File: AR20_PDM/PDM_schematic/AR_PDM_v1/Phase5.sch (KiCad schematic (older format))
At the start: 12 parts, among them Q5 BTS50025-1TAD, U7 INA233

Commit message: Alpha version DONE! - Gerber files generated
- Tweeked
- checked and re cheked
- added all missing components
- Created a really nice silkscreen
- Ready To Test
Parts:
- renumbered C_in2 to C17, C_out2 to C18, C_vs2 to C19, Cs2 to C20, C_bypass5 to C21, Q5 to Q3, R8 to R14, R_in2 to R15, R_sense2 to R16, R_s2 to R17, R_Shunt6 to R18, U7 to U4

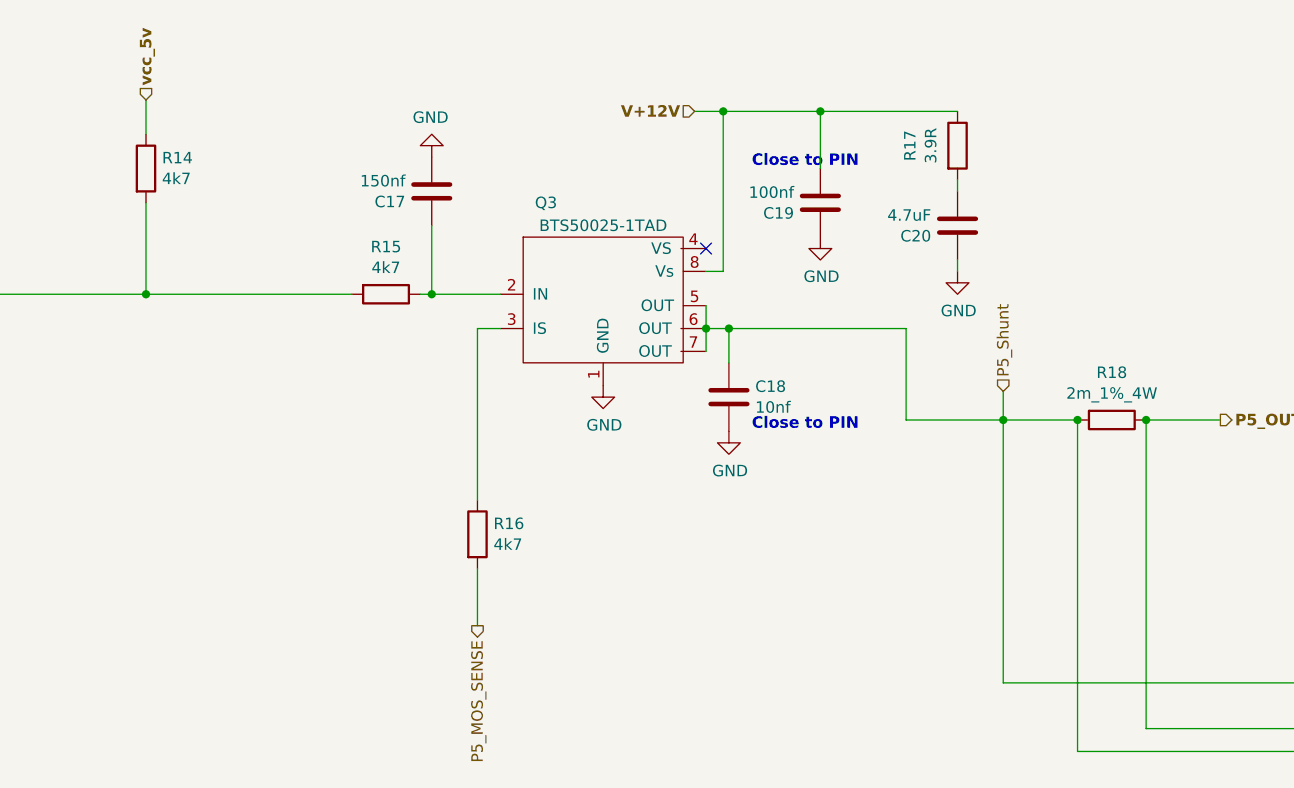
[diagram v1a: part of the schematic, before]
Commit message: Fixed wrong resistors, mos sense. Gerber files updated
- removed all R_is_protection resistors on each mosfet line
- added one R_is_protection resistors to mos_sense_all
ps, mux N-fets, does not need overvoltage protection. 60 volt tolerant.
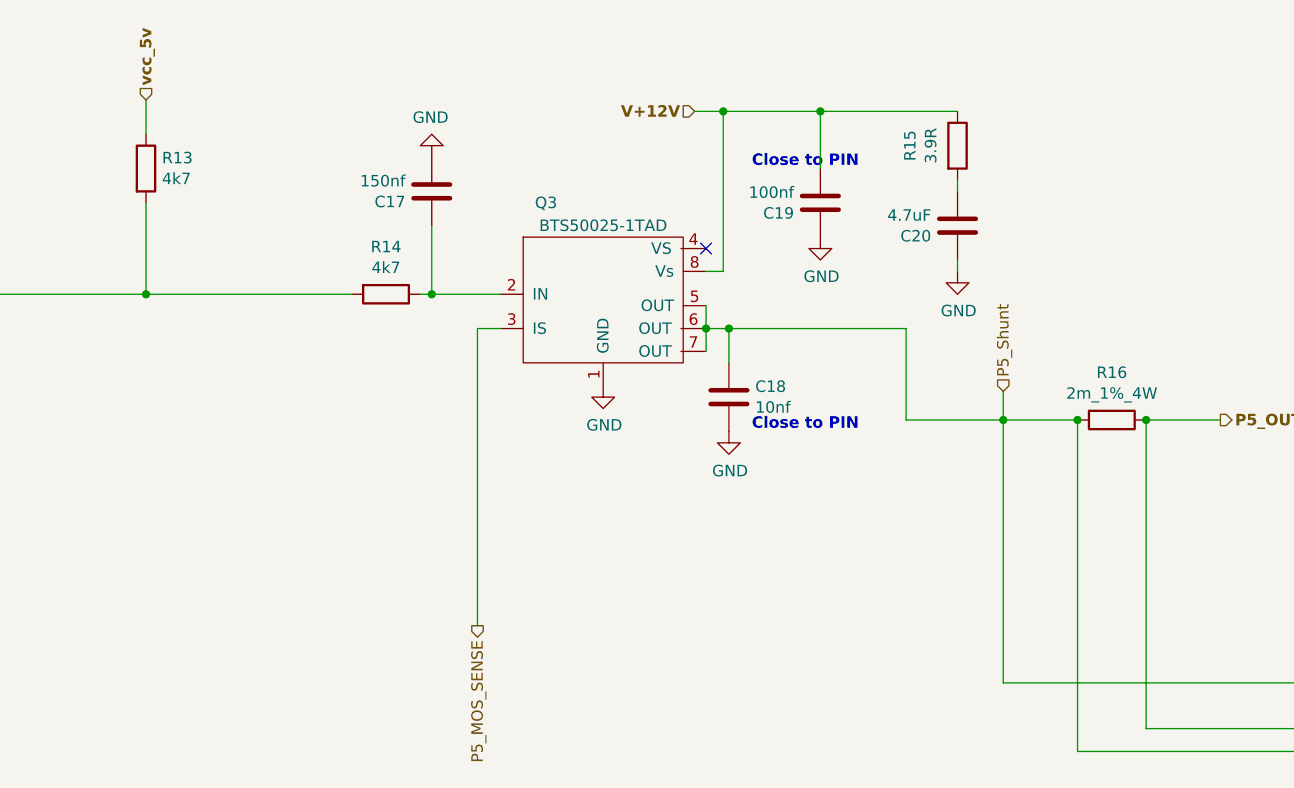
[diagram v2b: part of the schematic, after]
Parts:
- removed R16: 4k7, Resistor_SMD:R_0603_1608Metric, symbol AR20_PDM_v1-rescue:R-Device
- renumbered R14 to R13, R15 to R14, R17 to R15, R18 to R16
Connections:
- net P5_MOS_SENSE: now also Q3.3 (IS)
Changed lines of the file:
@@
 AR Path="/5E0FBBBD/5E21B80A" Ref="R?"  Part="1"
 AR Path="/5E0FC3A2/5E21B80A" Ref="R?"  Part="1"
-AR Path="/5E0FCFDC/5E21B80A" Ref="R15"  Part="1"
+AR Path="/5E0FCFDC/5E21B80A" Ref="R14"  Part="1"
 AR Path="/5E0FDCCC/5E21B80A" Ref="R?"  Part="1"
 AR Path="/5E10174B/5E21B80A" Ref="R?"  Part="1"
-F 0 "R15" V 3093 2400 50  0000 C CNN
+F 0 "R14" V 3093 2400 50  0000 C CNN
 F 1 "4k7" V 3184 2400 50  0000 C CNN
 F 2 "Resistor_SMD:R_0603_1608Metric" V 3230 2400 50  0001 C CNN
@@
 AR Path="/5E0FBBBD/5E21B81D" Ref="R?"  Part="1"
 AR Path="/5E0FC3A2/5E21B81D" Ref="R?"  Part="1"
-AR Path="/5E0FCFDC/5E21B81D" Ref="R14"  Part="1"
+AR Path="/5E0FCFDC/5E21B81D" Ref="R13"  Part="1"
 AR Path="/5E0FDCCC/5E21B81D" Ref="R?"  Part="1"
 AR Path="/5E10174B/5E21B81D" Ref="R?"  Part="1"
-F 0 "R14" H 2320 1896 50  0000 L CNN
+F 0 "R13" H 2320 1896 50  0000 L CNN
 F 1 "4k7" H 2320 1805 50  0000 L CNN
 F 2 "Resistor_SMD:R_0603_1608Metric" V 2180 1850 50  0001 C CNN
@@
 	3700 2550 3800 2550
 Wire Wire Line
-	3700 3850 3700 3600
-Wire Wire Line
 	8750 2850 8750 3350
 Wire Wire Line
@@
 AR Path="/5E0FBBBD/5E21B871" Ref="R?"  Part="1"
 AR Path="/5E0FC3A2/5E21B871" Ref="R?"  Part="1"
-AR Path="/5E0FCFDC/5E21B871" Ref="R17"  Part="1"
+AR Path="/5E0FCFDC/5E21B871" Ref="R15"  Part="1"
 AR Path="/5E0FDCCC/5E21B871" Ref="R?"  Part="1"
 AR Path="/5E10174B/5E21B871" Ref="R?"  Part="1"
-F 0 "R17" V 5593 1750 50  0000 C CNN
+F 0 "R15" V 5593 1750 50  0000 C CNN
 F 1 "3.9R" V 5684 1750 50  0000 C CNN
 F 2 "Resistor_SMD:R_0603_1608Metric" V 5730 1750 50  0001 C CNN
@@
 Wire Wire Line
 	6000 4100 8750 4100
-$Comp
-L AR20_PDM_v1-rescue:R-Device R?
-U 1 1 5E21B874
-P 3700 3450
-AR Path="/5DA89415/5E21B874" Ref="R?"  Part="1"
-AR Path="/5DEB10A1/5E21B874" Ref="R?"  Part="1"
-AR Path="/5DEB20EA/5E21B874" Ref="R?"  Part="1"
-AR Path="/5E0E4725/5E21B874" Ref="R?"  Part="1"
-AR Path="/5E0E4A93/5E21B874" Ref="R?"  Part="1"
-AR Path="/5E0E4EB5/5E21B874" Ref="R?"  Part="1"
-AR Path="/5E0E5304/5E21B874" Ref="R?"  Part="1"
-AR Path="/5E0E594B/5E21B874" Ref="R?"  Part="1"
-AR Path="/5E0E607C/5E21B874" Ref="R?"  Part="1"
-AR Path="/5E0FB5C8/5E21B874" Ref="R?"  Part="1"
-AR Path="/5E0FBBBD/5E21B874" Ref="R?"  Part="1"
-AR Path="/5E0FC3A2/5E21B874" Ref="R?"  Part="1"
-AR Path="/5E0FCFDC/5E21B874" Ref="R16"  Part="1"
-AR Path="/5E0FDCCC/5E21B874" Ref="R?"  Part="1"
-AR Path="/5E10174B/5E21B874" Ref="R?"  Part="1"
-F 0 "R16" H 3770 3496 50  0000 L CNN
-F 1 "4k7" H 3770 3405 50  0000 L CNN
-F 2 "Resistor_SMD:R_0603_1608Metric" V 3630 3450 50  0001 C CNN
-F 3 "~" H 3700 3450 50  0001 C CNN
-	1    3700 3450
-	1    0    0    -1
-$EndComp
 Wire Wire Line
 	6325 4400 8750 4400
@@
 AR Path="/5E0FBBBD/5E1D54E4" Ref="R?"  Part="1"
 AR Path="/5E0FC3A2/5E1D54E4" Ref="R?"  Part="1"
-AR Path="/5E0FCFDC/5E1D54E4" Ref="R18"  Part="1"
+AR Path="/5E0FCFDC/5E1D54E4" Ref="R16"  Part="1"
 AR Path="/5E0FDCCC/5E1D54E4" Ref="R?"  Part="1"
 AR Path="/5E10174B/5E1D54E4" Ref="R?"  Part="1"
-F 0 "R18" V 6268 2950 50  0000 C CNN
+F 0 "R16" V 6268 2950 50  0000 C CNN
 F 1 "2m_1%_4W" V 6359 2950 50  0000 C CNN
 F 2 "Resistor_SMD:R_2512_6332Metric" V 6405 2950 50  0001 C CNN
@@
 Connection ~ 6000 2950
 Wire Wire Line
-	3700 2550 3700 3300
-Wire Wire Line
 	4650 1600 4775 1600
 Wire Wire Line
@@
 Wire Wire Line
 	4775 1600 5200 1600
+Wire Wire Line
+	3700 2550 3700 3850
 $EndSCHEMATC

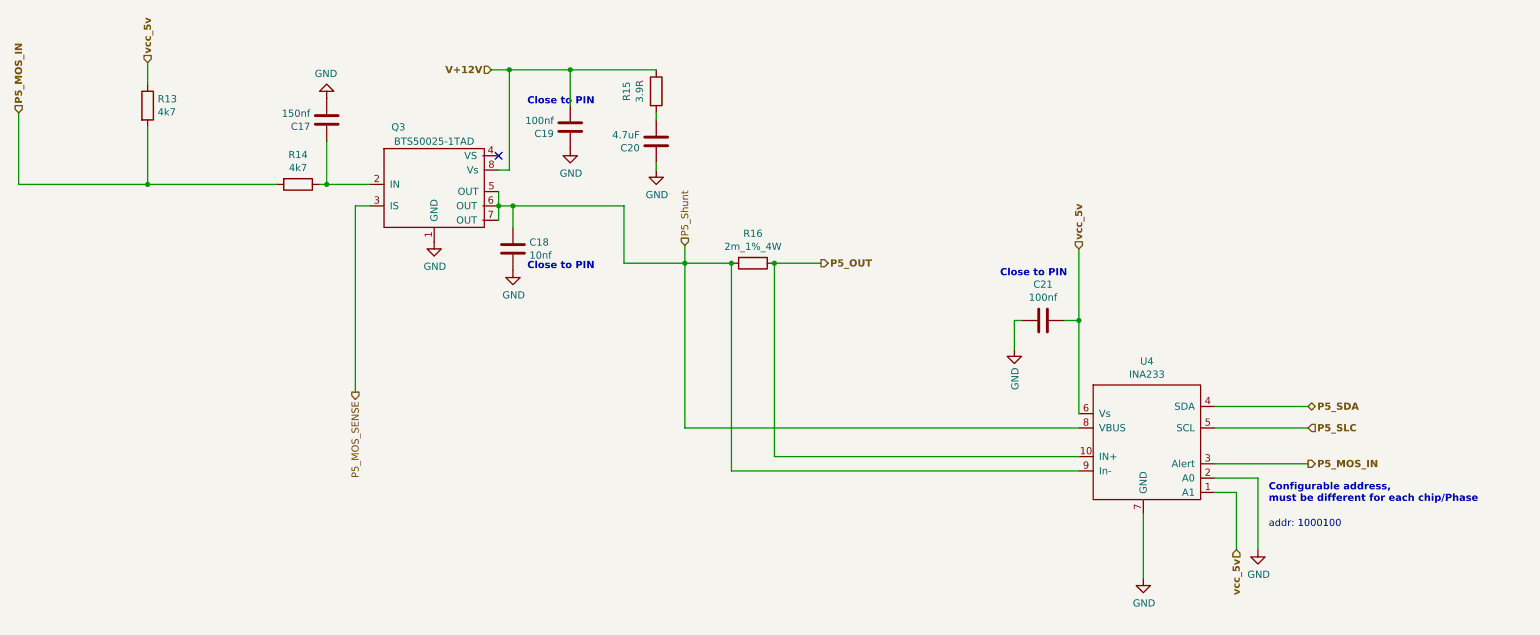
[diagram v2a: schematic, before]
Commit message: Major redesign. schematics completed, PCB work in progress
-TODO : A proper changelog file. Where all changes will apear 
- Redesigned schematics to accommodate errors in the improvement list
- More detail in ALPHA improvement list
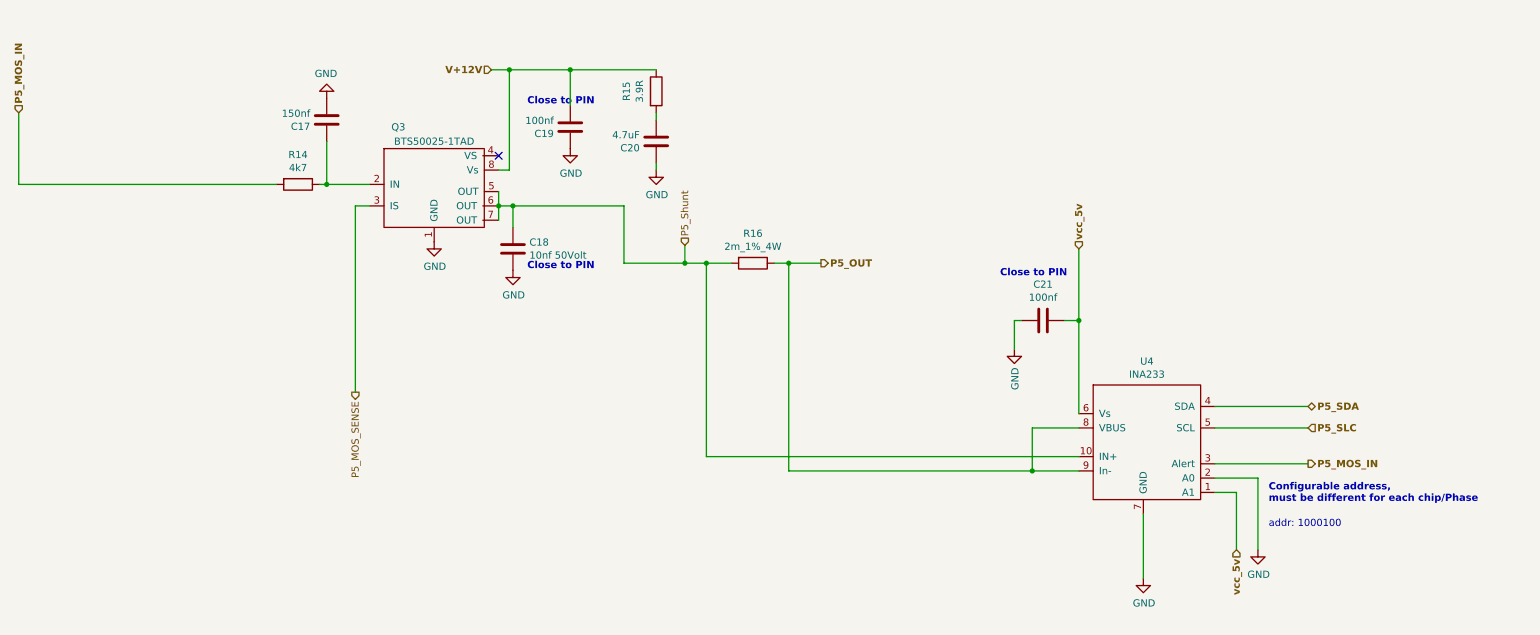
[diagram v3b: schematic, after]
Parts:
- removed R13: 4k7, Resistor_SMD:R_0603_1608Metric, symbol AR20_PDM_v1-rescue:R-Device
- C18: value 10nf -> 10nf 50Volt
- R15: footprint Resistor_SMD:R_0603_1608Metric -> Resistor_SMD:R_2512_6332Metric
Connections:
- net P5_OUT: now also U4.8 (VBUS), U4.9 (In-); no longer U4.10 (IN+)
- net P5_Shunt: now also U4.10 (IN+); no longer U4.8 (VBUS), U4.9 (In-)
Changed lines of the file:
@@
 $Descr A4 11693 8268
 encoding utf-8
-Sheet 4 13
+Sheet 4 14
 Title ""
 Date ""
@@
 AR Path="/5E10174B/5E21B810" Ref="C?"  Part="1"
 F 0 "C18" H 4915 2896 50  0000 L CNN
-F 1 "10nf" H 4915 2805 50  0000 L CNN
+F 1 "10nf 50Volt" H 4915 2805 50  0000 L CNN
 F 2 "Capacitor_SMD:C_0603_1608Metric" H 4838 2700 50  0001 C CNN
 F 3 "~" H 4800 2850 50  0001 C CNN
@@
 $EndComp
 $Comp
-L AR20_PDM_v1-rescue:R-Device R?
-U 1 1 5E21B81D
-P 2250 1850
-AR Path="/5DA89415/5E21B81D" Ref="R?"  Part="1"
-AR Path="/5DEB10A1/5E21B81D" Ref="R?"  Part="1"
-AR Path="/5DEB20EA/5E21B81D" Ref="R?"  Part="1"
-AR Path="/5E0E4725/5E21B81D" Ref="R?"  Part="1"
-AR Path="/5E0E4A93/5E21B81D" Ref="R?"  Part="1"
-AR Path="/5E0E4EB5/5E21B81D" Ref="R?"  Part="1"
-AR Path="/5E0E5304/5E21B81D" Ref="R?"  Part="1"
-AR Path="/5E0E594B/5E21B81D" Ref="R?"  Part="1"
-AR Path="/5E0E607C/5E21B81D" Ref="R?"  Part="1"
-AR Path="/5E0FB5C8/5E21B81D" Ref="R?"  Part="1"
-AR Path="/5E0FBBBD/5E21B81D" Ref="R?"  Part="1"
-AR Path="/5E0FC3A2/5E21B81D" Ref="R?"  Part="1"
-AR Path="/5E0FCFDC/5E21B81D" Ref="R13"  Part="1"
-AR Path="/5E0FDCCC/5E21B81D" Ref="R?"  Part="1"
-AR Path="/5E10174B/5E21B81D" Ref="R?"  Part="1"
-F 0 "R13" H 2320 1896 50  0000 L CNN
-F 1 "4k7" H 2320 1805 50  0000 L CNN
-F 2 "Resistor_SMD:R_0603_1608Metric" V 2180 1850 50  0001 C CNN
-F 3 "~" H 2250 1850 50  0001 C CNN
-	1    2250 1850
-	1    0    0    -1
-$EndComp
-$Comp
 L AR20_PDM_v1-rescue:C-Device C?
 U 1 1 5E21B825
@@
 Text Notes 8200 3050 0    50   ~ 10
 Close to PIN
-Text HLabel 2250 1550 1    50   Input ~ 10
-vcc_5v
 Wire Wire Line
 	9700 4100 10350 4100
-Wire Wire Line
-	2250 1550 2250 1700
 $Comp
 L AR20_PDM_v1-rescue:C-Device C?
@@
 F 0 "R15" V 5593 1750 50  0000 C CNN
 F 1 "3.9R" V 5684 1750 50  0000 C CNN
-F 2 "Resistor_SMD:R_0603_1608Metric" V 5730 1750 50  0001 C CNN
+F 2 "Resistor_SMD:R_2512_6332Metric" V 5730 1750 50  0001 C CNN
 F 3 "~" H 5800 1750 50  0001 C CNN
 	1    5800 1750
@@
 Wire Wire Line
 	9700 4350 10350 4350
-Connection ~ 2250 2400
-Wire Wire Line
-	2250 2000 2250 2400
 Wire Wire Line
 	1350 1900 1350 2400
-Wire Wire Line
-	1350 2400 2250 2400
 Wire Wire Line
 	10000 4450 10000 4950
@@
 	5575 2550 5575 2950
 Connection ~ 4800 2550
-Wire Wire Line
-	6000 4100 8750 4100
-Wire Wire Line
-	6325 4400 8750 4400
-Wire Wire Line
-	6625 4300 8750 4300
 Text HLabel 3700 3850 3    50   Output ~ 0
 P5_MOS_SENSE
-Wire Wire Line
-	6000 4100 6000 2950
 Wire Wire Line
 	5575 2950 6000 2950
@@
 V+12V
 Wire Wire Line
-	2250 2400 3150 2400
-Wire Wire Line
-	6625 2950 6625 4300
-Wire Wire Line
-	6325 2950 6325 4400
-Wire Wire Line
-	6000 2950 6325 2950
+	6000 2950 6150 2950
 $Comp
 L AR20_PDM_v1-rescue:R-Device R?
@@
 $EndComp
 Wire Wire Line
-	6625 2950 6950 2950
-Connection ~ 6325 2950
-Connection ~ 6625 2950
+	6625 2950 6725 2950
 Wire Wire Line
 	9200 4700 9200 5150
@@
 Wire Wire Line
 	3700 2550 3700 3850
+Wire Wire Line
+	1350 2400 3150 2400
+Wire Wire Line
+	8750 4300 6150 4300
+Wire Wire Line
+	6150 4300 6150 2950
+Wire Wire Line
+	8750 4400 8425 4400
+Wire Wire Line
+	8750 4100 8425 4100
+Wire Wire Line
+	8425 4100 8425 4400
+Connection ~ 8425 4400
+Wire Wire Line
+	8425 4400 6725 4400
+Wire Wire Line
+	6725 4400 6725 2950
+Connection ~ 6725 2950
+Wire Wire Line
+	6725 2950 6950 2950
+Connection ~ 6150 2950
+Wire Wire Line
+	6150 2950 6325 2950
 $EndSCHEMATC

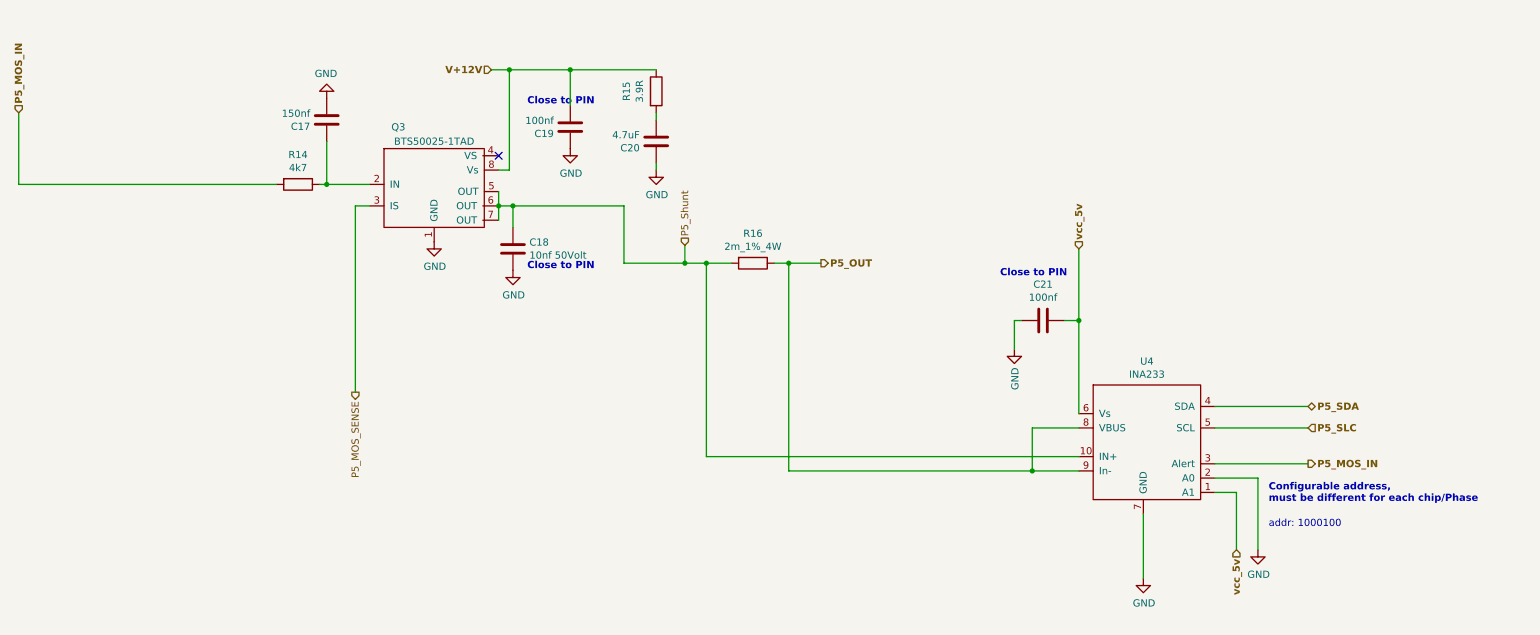
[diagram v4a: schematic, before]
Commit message: schematics rework
Fixed INA233 frying due to inductive flyback:
- Paced ina233 high side of the mosftets
- New input protection reseistors, and zener diodes, on each ina233.
Simplified:
- Removed the MUX and mos sense lines, as i realize that most of this functionality can be obtained trough INA233.
- Removed some of the cappacitors , besides the most needed ones.
- removed  back to back zener diode configuration, now a single diode insted.
 to reduce negative voltage in case of loss of VS, to be easy on the INA233 filters.
new stuff:
- Another temp sensor.
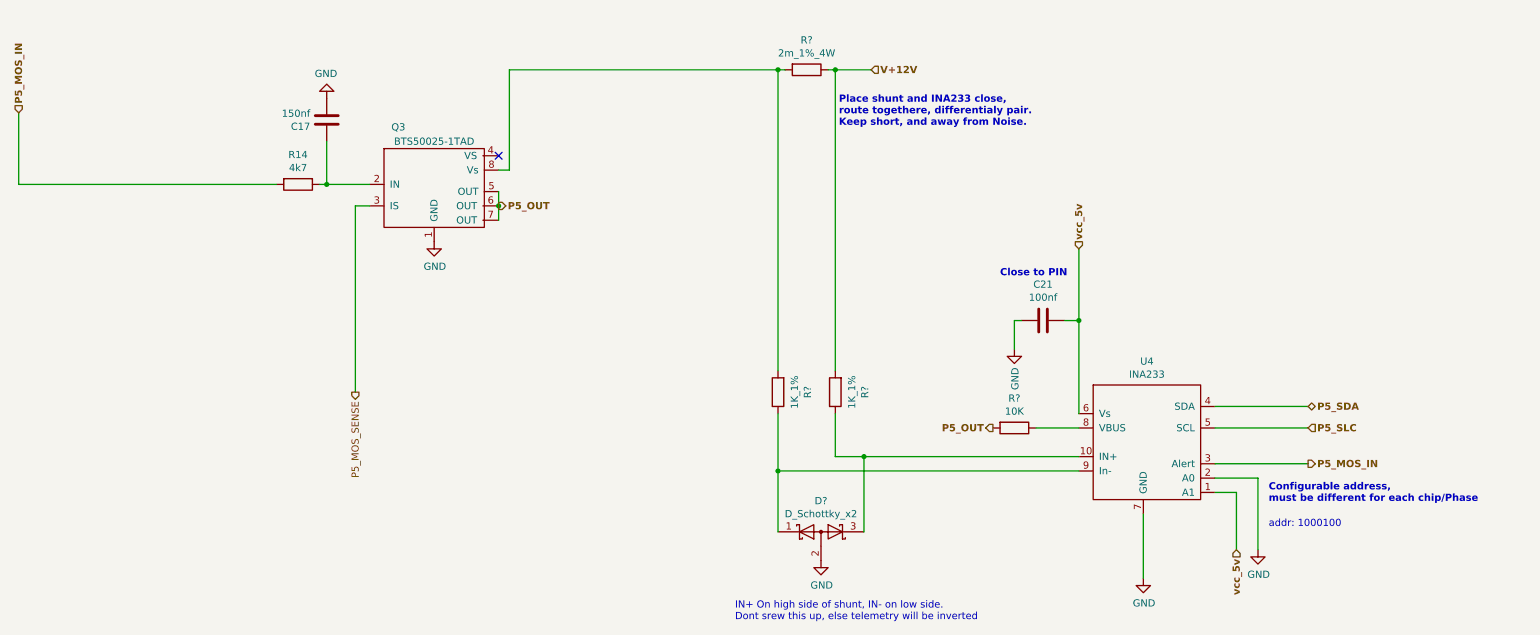
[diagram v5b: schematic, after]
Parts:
- removed C18: 10nf 50Volt, Capacitor_SMD:C_0603_1608Metric, symbol AR20_PDM_v1-rescue:C-Device
- removed C19: 100nf, Capacitor_SMD:C_0603_1608Metric, symbol AR20_PDM_v1-rescue:C-Device
- removed C20: 4.7uF, Capacitor_SMD:C_1206_3216Metric, symbol AR20_PDM_v1-rescue:C-Device
- removed R15: 3.9R, Resistor_SMD:R_2512_6332Metric, symbol AR20_PDM_v1-rescue:R-Device
- removed R16: 2m_1%_4W, Resistor_SMD:R_2512_6332Metric, symbol AR20_PDM_v1-rescue:R-Device
- added D?: D_Schottky_x2, symbol AR20_PDM_v1-rescue:D_Schottky_x2
- added R?: 2m_1%_4W, Resistor_SMD:R_2512_6332Metric, symbol AR20_PDM_v1-rescue:R-Device
- added R? (x2): 1K_1%, Resistor_SMD:R_0603_1608Metric, symbol AR20_PDM_v1-rescue:R-Device
- added R?: 10K, Resistor_SMD:R_0603_1608Metric, symbol AR20_PDM_v1-rescue:R-Device
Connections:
- net GND: now also D?.2 (A)
- net P5_OUT: now also Q3.5 (OUT), Q3.6 (OUT), Q3.7 (OUT), R?.2; no longer U4.8 (VBUS), U4.9 (In-)
- net V+12V: now also R?.1, R?.2; no longer Q3.8 (Vs)
- removed net P5_Shunt: Q3.5 (OUT), Q3.6 (OUT), Q3.7 (OUT), U4.10 (IN+)
- new net: Q3.8 (Vs), R?.2, R?.2
- new net: D?.3 (K), R?.1, U4.10 (IN+)
- new net: R?.1, U4.8 (VBUS)
- new net: D?.1 (K), R?.1, U4.9 (In-)
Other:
- note added: "IN+ On high side of shunt, IN- on low side.\nDont srew this up, else telemetry will be inverted"
- note added: "Place shunt and INA233 close, \nroute togethere, differentialy pair. \nKeep short, and away from Noise."
